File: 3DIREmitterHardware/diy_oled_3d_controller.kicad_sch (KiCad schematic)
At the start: 20 parts, among them Q1 AO3400A, U1 OPT101P, U2 OPT101P

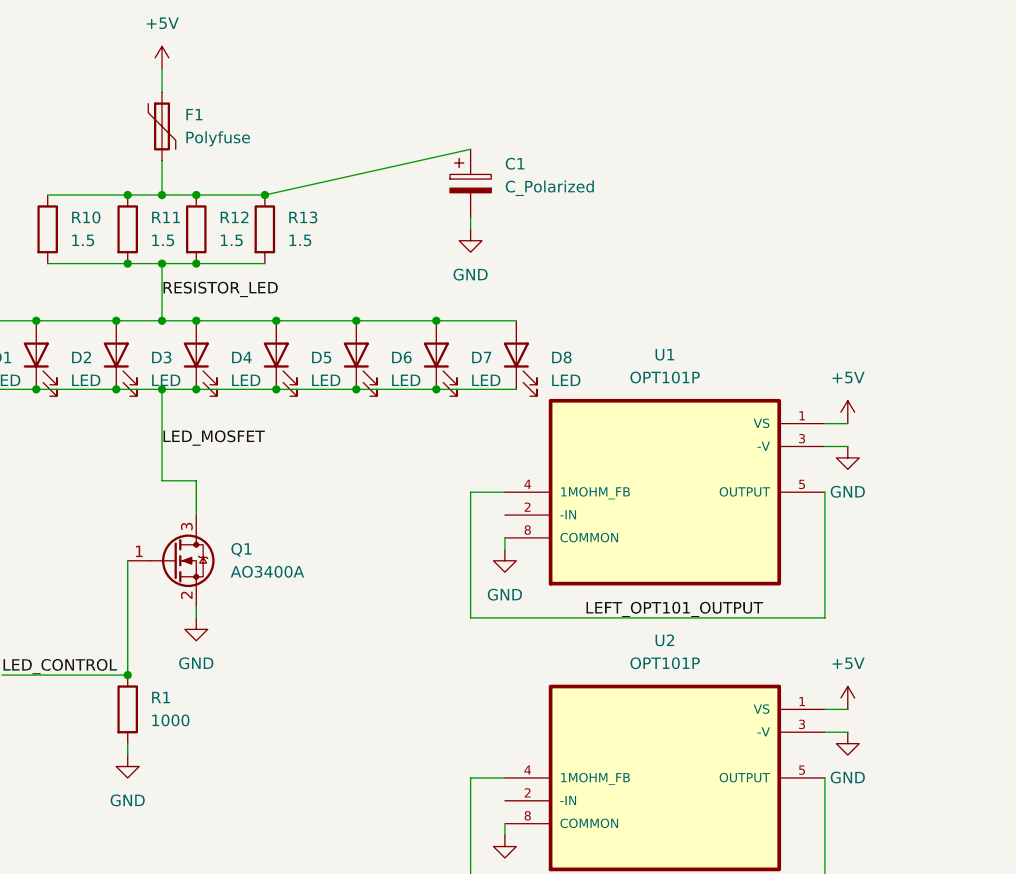
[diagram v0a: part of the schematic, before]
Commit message: fixed fillzone in hardware pcb design wasn't connected to 5V_AFTER_FUSE
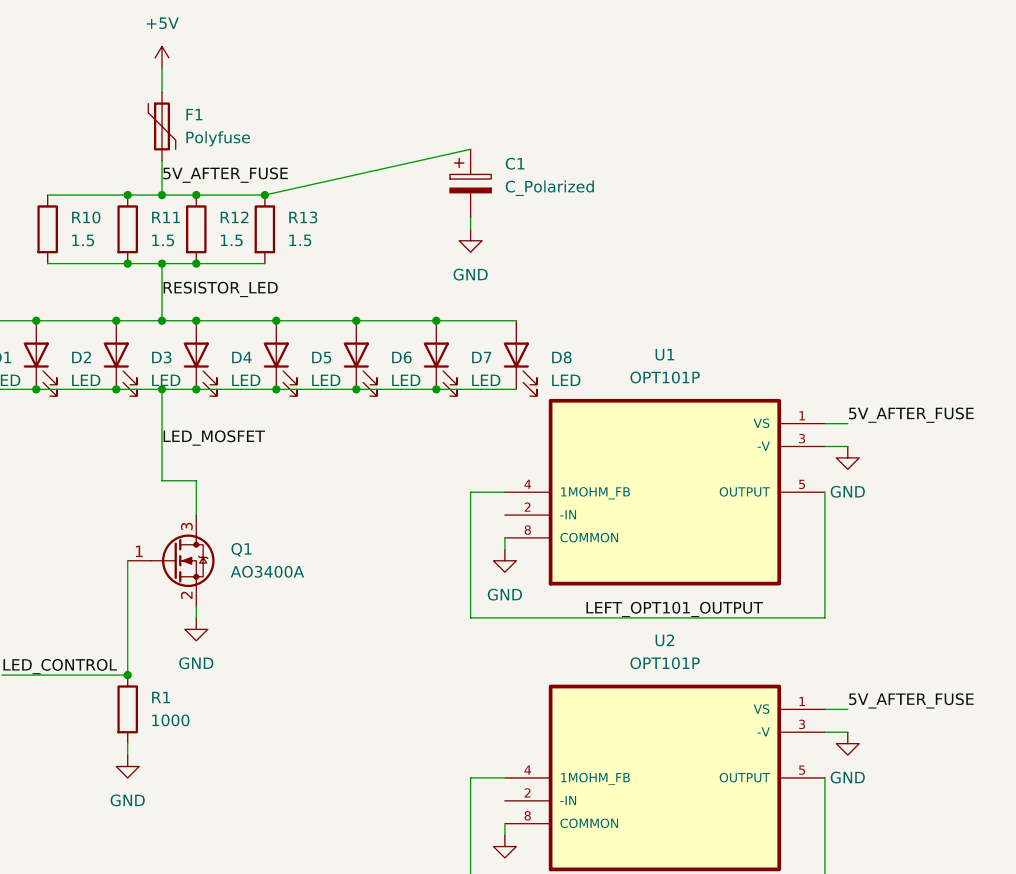
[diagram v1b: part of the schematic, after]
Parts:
- F1: footprint (none) -> Fuse:Fuse_0805_2012Metric_Pad1.15x1.40mm_HandSolder
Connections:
- net +5V: no longer U1.1 (VS), U2.1 (VS)
- net 5V_AFTER_FUSE: now reaches C1.1, F1.2, R10.1, R11.1, R12.1, R13.1
- net 5V_AFTER_FUSE: now also U1.1 (VS), U2.1 (VS)
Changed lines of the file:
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@@
+    (effects (font (size 1.27 1.27)) (justify left bottom))
+  )
+  (label "5V_AFTER_FUSE" (at 176.53 43.18 0) (fields_autoplaced)
     (effects (font (size 1.27 1.27)) (justify left bottom))
   )
@@
     (effects (font (size 1.27 1.27)) (justify left bottom))
   )
+  (label "5V_AFTER_FUSE" (at 252.73 101.6 0) (fields_autoplaced)
+    (effects (font (size 1.27 1.27)) (justify left bottom))
+  )
   (label "LED_MOSFET" (at 176.53 72.39 0) (fields_autoplaced)
     (effects (font (size 1.27 1.27)) (justify left bottom))
   )
   (label "LED_CONTROL" (at 78.74 88.9 0) (fields_autoplaced)
+    (effects (font (size 1.27 1.27)) (justify left bottom))
+  )
+  (label "5V_AFTER_FUSE" (at 252.73 69.85 0) (fields_autoplaced)
     (effects (font (size 1.27 1.27)) (justify left bottom))
   )
@@
     )
   )
-  (symbol (lib_id "power:+5V") (at 252.73 69.85 0) (unit 1)
-    (in_bom yes) (on_board yes) (dnp no) (fields_autoplaced)
-    (property "Reference" "#PWR0109" (at 252.73 73.66 0)
-      (effects (font (size 1.27 1.27)) hide)
-    )
-    (property "Value" "+5V" (at 252.73 64.77 0)
-      (effects (font (size 1.27 1.27)))
-    )
-    (property "Footprint" "" (at 252.73 69.85 0)
-      (effects (font (size 1.27 1.27)) hide)
-    )
-    (property "Datasheet" "" (at 252.73 69.85 0)
-      (effects (font (size 1.27 1.27)) hide)
-    )
-    (pin "1")
-    (instances
-      (project "diy_oled_3d_controller"
-        (path "/e63e39d7-6ac0-4ffd-8aa3-1841a4541b55"
-          (reference "#PWR0109") (unit 1)
-        )
-      )
-    )
-  )
   (symbol (lib_id "power:+5V") (at 119.38 74.93 0) (unit 1)
     (in_bom yes) (on_board yes) (dnp no) (fields_autoplaced)
@@
       (effects (font (size 1.27 1.27)) (justify left))
     )
-    (property "Footprint" "" (at 177.8 41.91 0)
+    (property "Footprint" "Fuse:Fuse_0805_2012Metric_Pad1.15x1.40mm_HandSolder" (at 177.8 41.91 0)
       (effects (font (size 1.27 1.27)) (justify left) hide)
     )
@@
         )
       )
-    )
-  )
-  (symbol (lib_id "power:+5V") (at 252.73 101.6 0) (unit 1)
-    (in_bom yes) (on_board yes) (dnp no) (fields_autoplaced)
-    (property "Reference" "#PWR0107" (at 252.73 105.41 0)
-      (effects (font (size 1.27 1.27)) hide)
-    )
-    (property "Value" "+5V" (at 252.73 96.52 0)
-      (effects (font (size 1.27 1.27)))
-    )
-    (property "Footprint" "" (at 252.73 101.6 0)
-      (effects (font (size 1.27 1.27)) hide)
-    )
-    (property "Datasheet" "" (at 252.73 101.6 0)
-      (effects (font (size 1.27 1.27)) hide)
-    )
-    (pin "1")
-    (instances
-      (project "diy_oled_3d_controller"
-        (path "/e63e39d7-6ac0-4ffd-8aa3-1841a4541b55"
-          (reference "#PWR0107") (unit 1)
-        )
-      )

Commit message: initial v2 pcb hardware design
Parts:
- removed D5, D6, D7, D8: LED, LED_THT:LED_D5.0mm, symbol Device:LED
- added C2: C_Polarized, Capacitor_THT:C_Radial_D6.3mm_H11.0mm_P2.50mm, symbol Device:C_Polarized
- added C3, C4: 100nF, Capacitor_SMD:C_0603_1608Metric_Pad1.08x0.95mm_HandSolder, symbol Device:C
- added D10, D9: VBPW34S, VBPW34S:XDCR_VBPW34S, symbol VBPW34S:VBPW34S
- added D11, D12, D13, D14: LED, LED_SMD:LED_1210_3225Metric_Pad1.42x2.65mm_HandSolder, symbol Device:LED
- added H1, H2, H3, H4, H5, H6: MountingHole, Library:MountingHole_1.6mm_M1.4_ISO7380, symbol Mechanical:MountingHole
- added J1, J2, J3: Conn_01x06_Pin, Connector_PinHeader_2.54mm:PinHeader_1x06_P2.54mm_Vertical, symbol Connector:Conn_01x06_Pin
- added Q2: AO3400A, Package_TO_SOT_SMD:SOT-23, symbol Transistor_FET:AO3400A
- added R2, R3: 10k, Resistor_SMD:R_0603_1608Metric_Pad0.98x0.95mm_HandSolder, symbol Device:R
- added R4: 1000, Resistor_SMD:R_0603_1608Metric_Pad0.98x0.95mm_HandSolder, symbol Device:R
- added S2, S3, S4: TL3342F160QG, Tactile.Switch:SW_TL3342F160QG, symbol TactileSwitch:TL3342F160QG
- added U4: MCP6022-I_SN, MCP6022-I_SN:SOIC127P599X175-8N, symbol MCP6022-I_SN:MCP6022-I_SN
- D1, D2, D3, D4: footprint LED_THT:LED_D5.0mm -> LED_SMD:LED_1210_3225Metric_Pad1.42x2.65mm_HandSolder
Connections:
- net 5V_AFTER_FUSE: no longer U1.1 (VS), U2.1 (VS)
- net VCC_1: now reaches B1.21 (VCC)
- net VCC_1: now also C2.1, J1.3 (Pin_3)
- net at B1.5 (2): now also S2.1, S2.2
- net at B1.7 (4): now also S3.1, S3.2
- net at B1.8 (*5): now also S4.1, S4.2
- net +5V renamed +5V_1
- removed net GND: B1.23 (GND), C1.2, Q1.2 (S), R1.2, S1.3, S1.4, U1.3 (-V), U1.8 (COMMON), U2.3 (-V), U2.8 (COMMON)
- net LED_CONTROL renamed LED_CONTROL_2
- net LED_CONTROL_2: now also J2.4 (Pin_4); no longer B1.6 (*3)
- net LED_MOSFET renamed LED_MOSFET_2
- net LEFT_OPT101_OUTPUT renamed LEFT_SIGNAL_3
- net LEFT_SIGNAL_3: now also J3.5 (Pin_5); no longer B1.18 (A1)
- net RESISTOR_LED renamed LED_POWER_1
- net LED_POWER_1: now also J1.1 (Pin_1); no longer D1.2 (A), D2.2 (A), D3.2 (A), D4.2 (A)
- net RIGHT_OPT101_OUTPUT renamed RIGHT_SIGNAL_3
- net RIGHT_SIGNAL_3: now also J3.6 (Pin_6); no longer B1.17 (A0)
- new net: C4.2, D10.A, R3.1, U4.2 (VINA-)
- new net: C3.1, D9.A, R2.2, U4.6 (VINB-)
- new net GND1: B1.23 (GND), C1.2, C2.2, J1.2 (Pin_2), S1.3, S1.4, S2.3, S2.4, S3.3, S3.4, S4.3, S4.4
- new net GND2: D10.K, D9.K, J2.2 (Pin_2), Q1.2 (S), R1.2, U4.3 (VINA+), U4.4 (VSS), U4.5 (VINB+)
- new net GND3: J3.2 (Pin_2), Q2.2 (S), R4.2, U1.3 (-V), U1.8 (COMMON), U2.3 (-V), U2.8 (COMMON)
- new net LED_CONTROL_1: B1.6 (*3), J1.4 (Pin_4)
- new net LED_CONTROL_3: J3.4 (Pin_4), Q2.1 (G), R4.1
- new net LED_MOSFET_3: D11.1 (K), D12.1 (K), D13.1 (K), D14.1 (K), Q2.3 (D)
- new net LED_POWER_2: D1.2 (A), D2.2 (A), D3.2 (A), D4.2 (A), J2.1 (Pin_1)
- new net LED_POWER_3: D11.2 (A), D12.2 (A), D13.2 (A), D14.2 (A), J3.1 (Pin_1)
- new net LEFT_SIGNAL_1: B1.18 (A1), J1.5 (Pin_5)
- new net LEFT_SIGNAL_2: C4.1, J2.5 (Pin_5), R3.2, U4.1 (VOUTA)
- new net RIGHT_SIGNAL_1: B1.17 (A0), J1.6 (Pin_6)
- new net RIGHT_SIGNAL_2: C3.2, J2.6 (Pin_6), R2.1, U4.7 (VOUTB)
- new net VCC_2: J2.3 (Pin_3), U4.8 (VDD)
- new net VCC_3: J3.3 (Pin_3), U1.1 (VS), U2.1 (VS)
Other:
- moved on the sheet: B1, C1, D1, D2, D3, D4, F1, Q1, R1, R10, R11, R12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

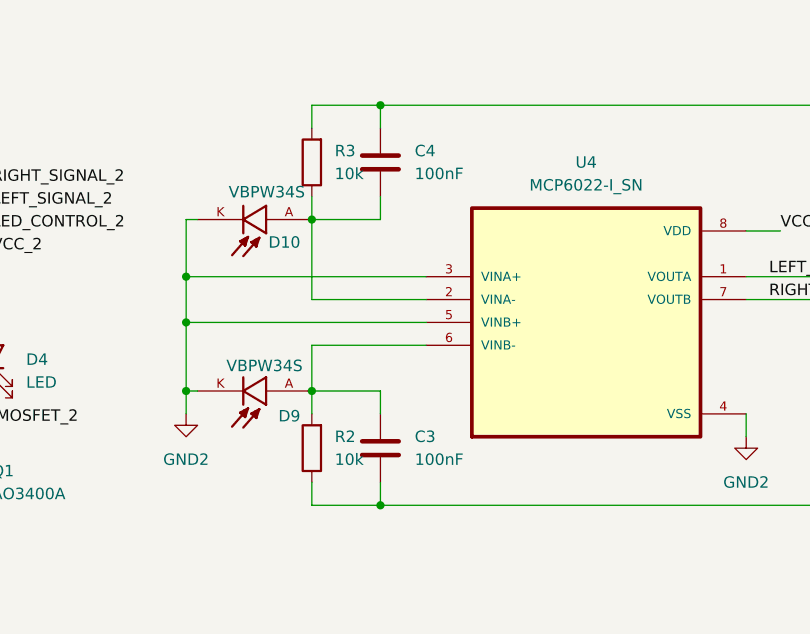
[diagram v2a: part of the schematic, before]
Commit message: some minor fixes to pcb schamtic values for opamp passives
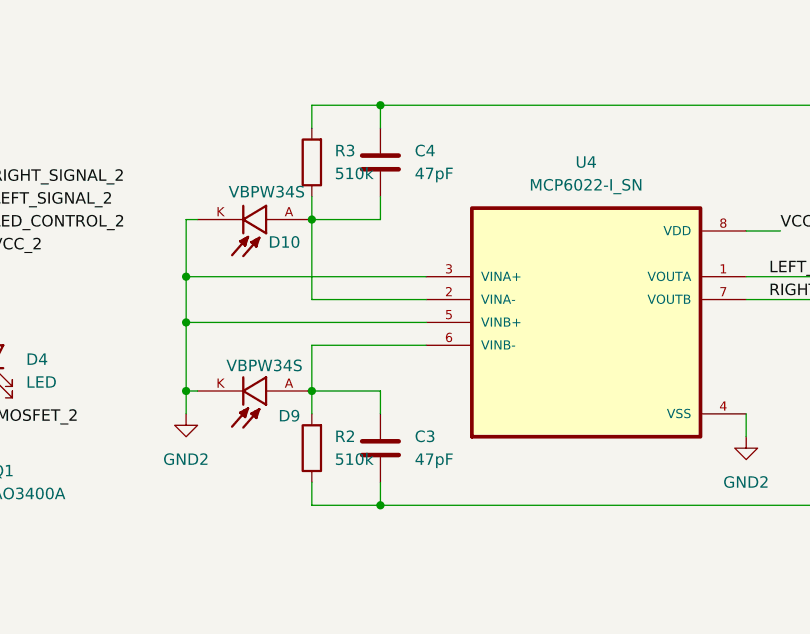
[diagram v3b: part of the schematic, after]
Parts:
- C3, C4: value 100nF -> 47pF
- R2, R3: value 10k -> 510k
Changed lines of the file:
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@@
 			)
 		)
-		(property "Value" "10k"
+		(property "Value" "510k"
 			(at 199.39 31.7499 0)
 			(effects
@@
 			)
 		)
-		(property "Value" "100nF"
+		(property "Value" "47pF"
 			(at 208.28 63.4999 0)
 			(effects
@@
 			)
 		)
-		(property "Value" "10k"
+		(property "Value" "510k"
 			(at 199.39 63.4999 0)
 			(effects
@@
 			)
 		)
-		(property "Value" "100nF"
+		(property "Value" "47pF"
 			(at 208.28 31.7499 0)
 			(effects
